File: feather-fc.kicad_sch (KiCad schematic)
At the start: 19 parts, among them M1 Motor_Servo, M2 Motor_Servo, M3 Motor_Servo, M4 Motor_Servo, M5 Motor_Servo, M6 Motor_Servo, M7 Motor_Servo, M8 Motor_Servo, SW1 Mode_SW, SW3 Bind_SW, U3 MCP1700-3302E/TO

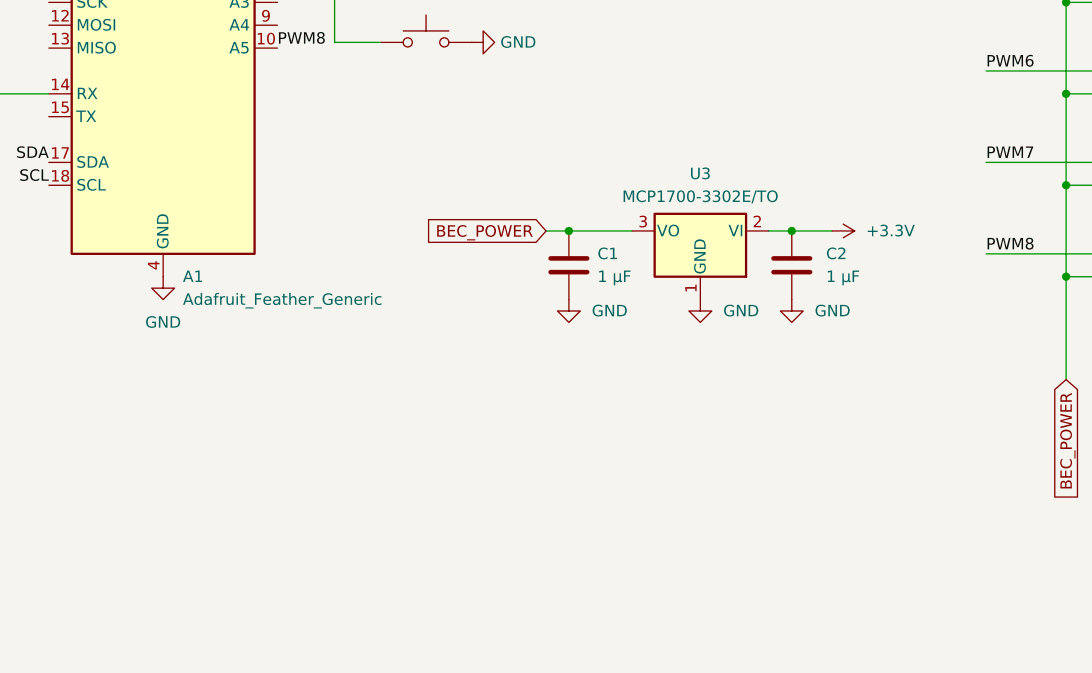
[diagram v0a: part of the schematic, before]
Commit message: Version 2: Fix the voltage regulator wiring
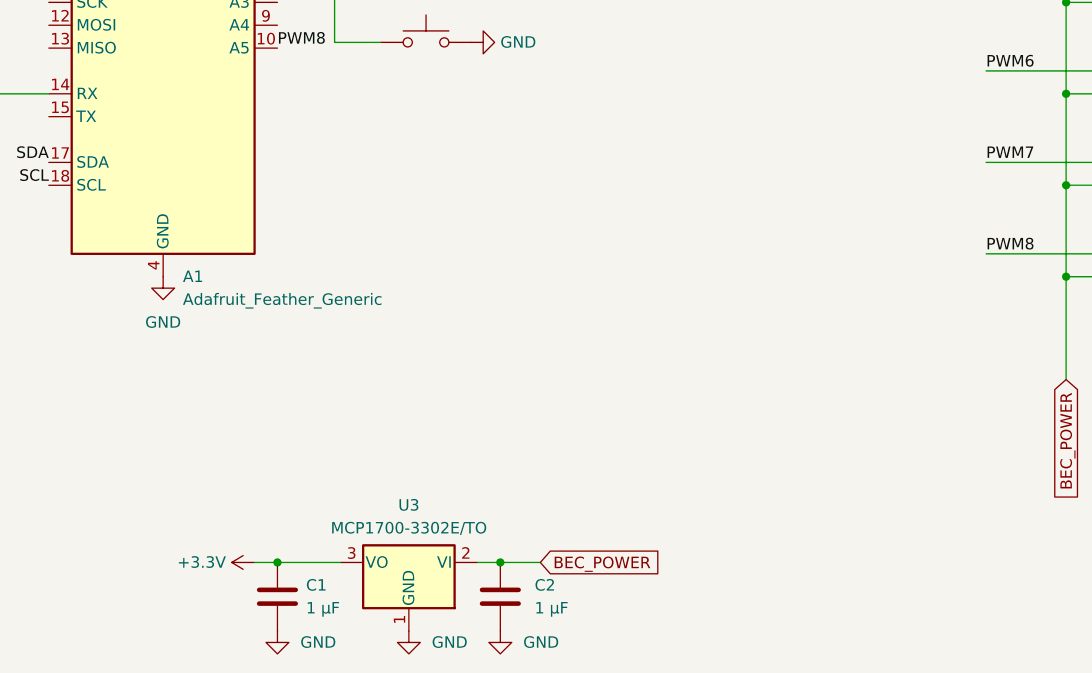
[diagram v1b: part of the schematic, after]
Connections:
- net +3.3V: now also C1.1, U3.3 (VO); no longer C2.1, U3.2 (VI)
- net BEC_POWER: now also C2.1, U3.2 (VI); no longer C1.1, U3.3 (VO)
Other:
- moved on the sheet: C1, C2, U3

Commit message: Version 3 layout 2
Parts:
- removed M8: Motor_Servo, Connector_PinHeader_2.54mm:PinHeader_1x03_P2.54mm_Vertical, symbol Custom_Symbols:Motor_Servo
- removed U4: ~, Connector_JST:JST_XH_B4B-XH-A_1x04_P2.50mm_Vertical, symbol Custom_Symbols:Stemma_QT_connector
- removed U5: ~, Connector_JST:JST_XH_B3B-XH-A_1x03_P2.50mm_Vertical, symbol Custom_Symbols:Spektrum_sattelite_reciever
- added D1: S2M-TP, Diode_SMD:D_SMB, symbol Device:D
- added JP2: SolderJumper_2_Open, Jumper:SolderJumper-2_P1.3mm_Open_RoundedPad1.0x1.5mm, symbol Jumper:SolderJumper_2_Open
- added SW3: Reset_SW, Button_Switch_THT:SW_PUSH_6mm, symbol Switch:SW_Push
- added U4: MCP1703Ax-300xxTT, Package_TO_SOT_SMD:SOT-23, symbol Regulator_Linear:MCP1703Ax-300xxTT
- renumbered SW3 to SW2
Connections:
- net +3.3V: now also A1.2 (3V3); no longer C1.1, U3.3 (VO)
- net BEC_POWER: now also D1.1 (K), JP2.2 (B); no longer M1.2 (+), M2.2 (+), M3.2 (+), M4.2 (+), M5.2 (+), M6.2 (+), M7.2 (+)
- net GND: now also SW3.2
- net at A1.1 (~{RESET}): now also SW3.1
- net at JP1.1 (A): now also C1.1, U3.3 (VO); no longer A1.2 (3V3)
- net PWM8: no longer names the net of A1.10 (A5)
- new net: D1.2 (A), JP2.1 (A), M1.2 (+), M2.2 (+), M3.2 (+), M4.2 (+), M5.2 (+), M6.2 (+), M7.2 (+)
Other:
- moved on the sheet: JP1

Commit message: Verion 3 final revision
General cleanup and rearrangement
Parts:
- removed U4: MCP1703Ax-300xxTT, Package_TO_SOT_SMD:SOT-23, symbol Regulator_Linear:MCP1703Ax-300xxTT
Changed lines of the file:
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@@
     (stroke (width 0) (type default))
-  )
-  (text_box "Second QT symbol is for JST XH connector"
-    (at 35.56 123.825 0) (size 44.45 3.81)
-    (stroke (width 0) (type default))
-    (fill (type none))
-    (effects (font (size 1.27 1.27)) (justify left top))
   )
   (label "PWM6" (at 219.71 78.74 0) (fields_autoplaced)
@@
         )
       )
-    )
-  )
-  (symbol (lib_id "Regulator_Linear:MCP1703Ax-300xxTT") (at 210.185 147.955 0) (unit 1)
-    (in_bom yes) (on_board yes) (dnp no) (fields_autoplaced)
-    (property "Reference" "U4" (at 210.185 140.97 0)
-      (effects (font (size 1.27 1.27)))
-    )
-    (property "Value" "MCP1703Ax-300xxTT" (at 210.185 143.51 0)
-      (effects (font (size 1.27 1.27)))
-    )
-    (property "Footprint" "Package_TO_SOT_SMD:SOT-23" (at 210.185 142.875 0)
-      (effects (font (size 1.27 1.27)) hide)
-    )
-    (property "Datasheet" "http://ww1.microchip.com/downloads/en/DeviceDoc/20005122B.pdf" (at 210.185 149.225 0)
-      (effects (font (size 1.27 1.27)) hide)
-    )
-    (pin "2")
-    (pin "1")
-    (pin "3")
-    (instances
-      (project "feather-fc"
-        (path "/f7324c5f-3518-424c-a106-fa35bf6a0487"
-          (reference "U4") (unit 1)
-        )
-      )
